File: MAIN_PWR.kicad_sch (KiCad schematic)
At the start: 0 parts

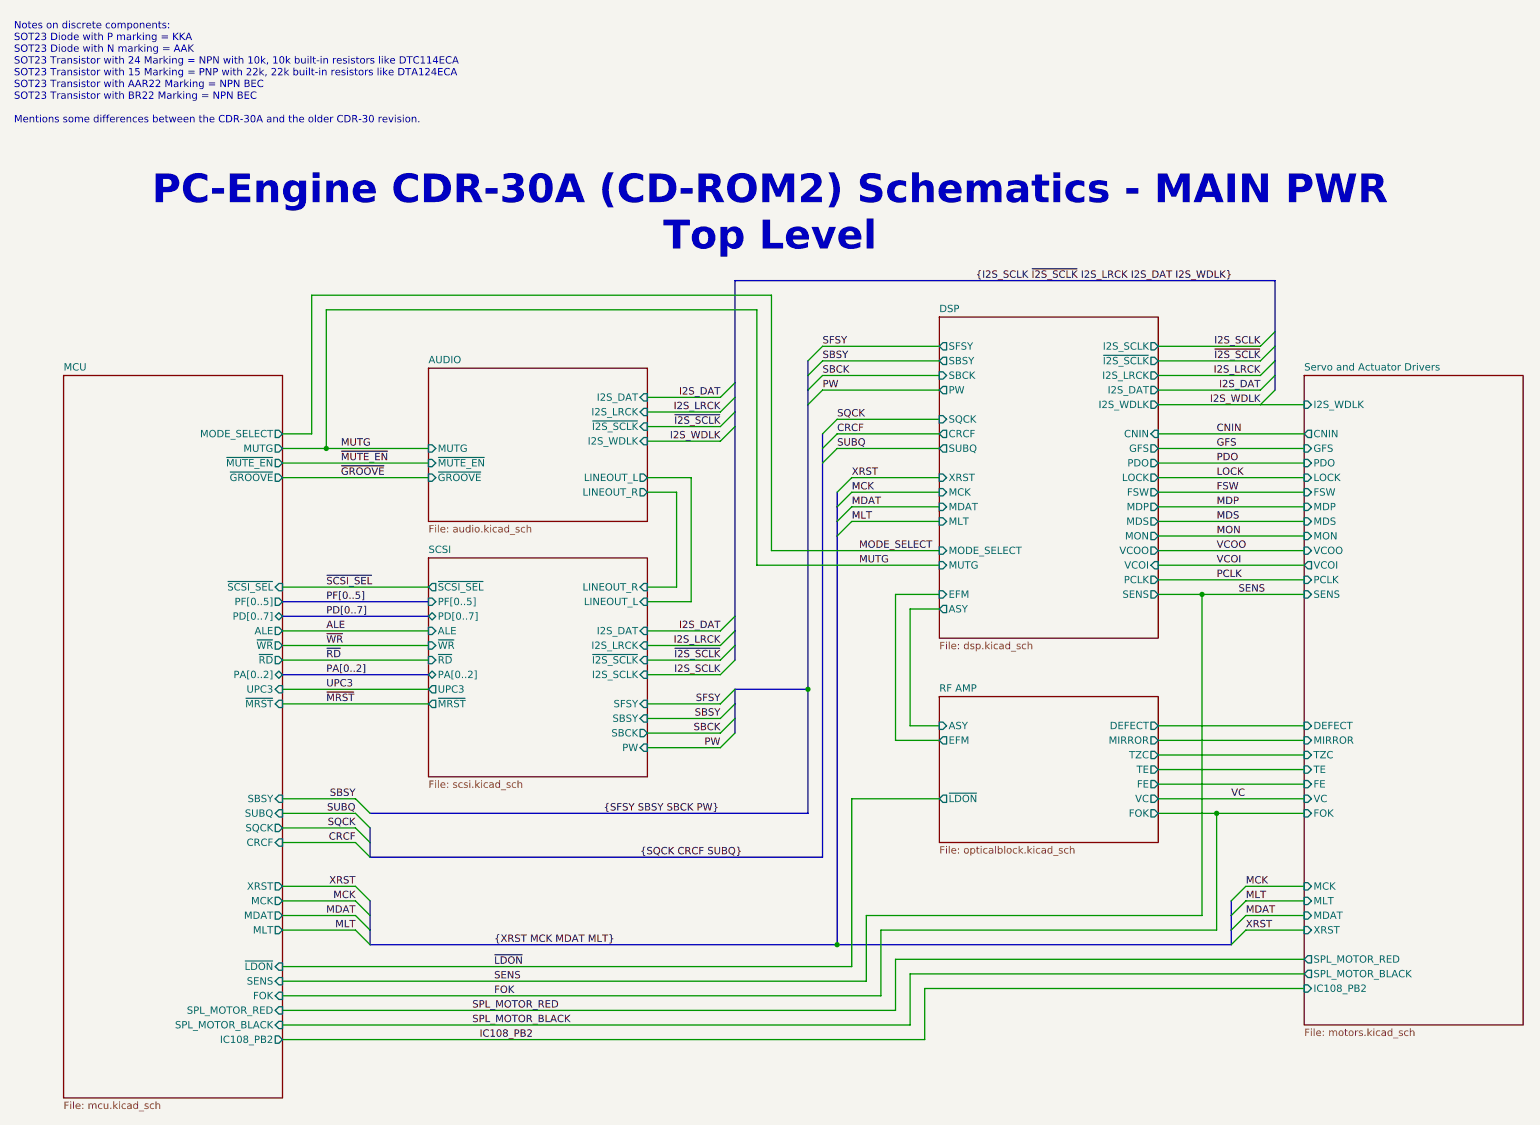
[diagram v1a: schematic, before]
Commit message: Small update, some typo fixes, more comments added to help understanding
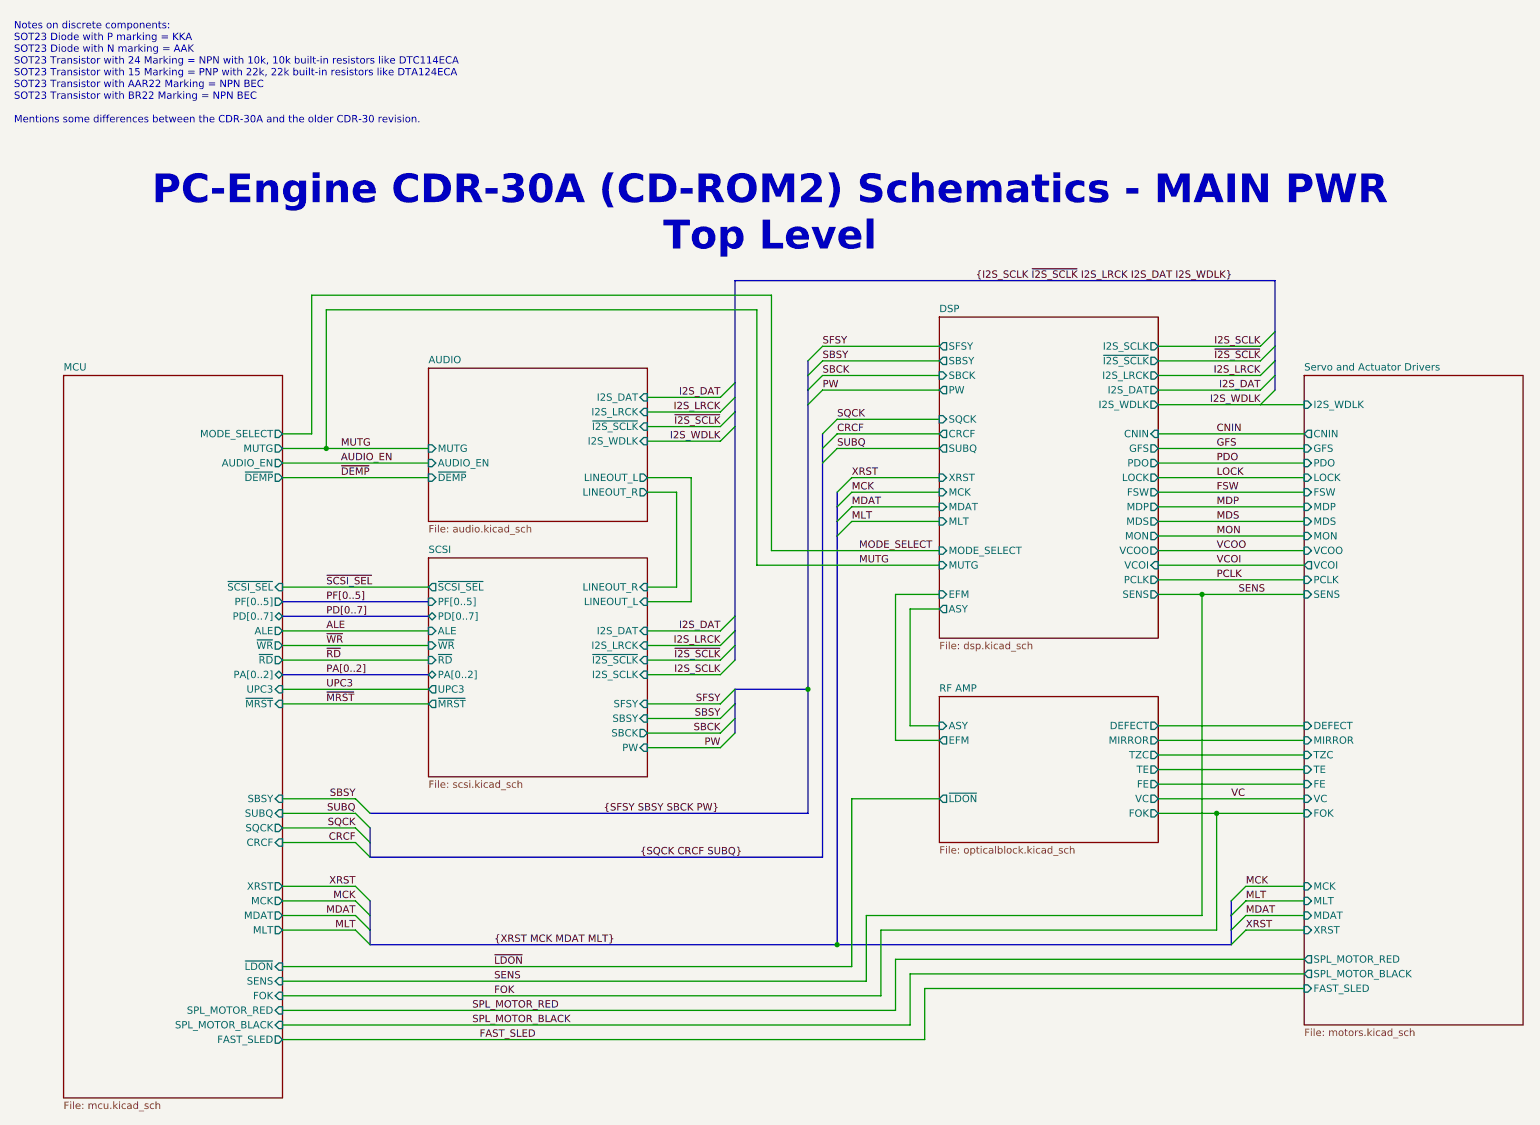
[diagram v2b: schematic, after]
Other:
- sheet AUDIO ports: added AUDIO_EN, ~{DEMP}; removed ~{GROOVE}, ~{MUTE_EN}
- sheet MCU ports: added AUDIO_EN, FAST_SLED, ~{DEMP}; removed IC108_PB2, ~{GROOVE}, ~{MUTE_EN}
- sheet Servo and Actuator Drivers ports: added FAST_SLED; removed IC108_PB2
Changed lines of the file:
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@@
 		)
 	)
-	(label "~{GROOVE}"
+	(label "~{DEMP}"
 		(at 73.66 68.58 0)
 		(fields_autoplaced yes)
@@
 		)
 	)
-	(label "IC108_PB2"
+	(label "FAST_SLED"
 		(at 97.79 166.37 0)
 		(fields_autoplaced yes)
@@
 		)
 	)
-	(label "~{MUTE_EN}"
+	(label "AUDIO_EN"
 		(at 73.66 66.04 0)
 		(fields_autoplaced yes)
@@
 			)
 		)
-		(pin "~{GROOVE}" output
+		(pin "~{DEMP}" output
 			(at 63.5 68.58 0)
 			(effects
@@
 			)
 		)
-		(pin "IC108_PB2" output
+		(pin "FAST_SLED" output
 			(at 63.5 166.37 0)
 			(effects
@@
 			)
 		)
-		(pin "~{MUTE_EN}" output
+		(pin "AUDIO_EN" output
 			(at 63.5 66.04 0)
 			(effects
@@
 			)
 		)
-		(pin "IC108_PB2" input
+		(pin "FAST_SLED" input
 			(at 241.3 157.48 180)
 			(effects
@@
 			)
 		)
-		(pin "~{MUTE_EN}" input
+		(pin "AUDIO_EN" input
 			(at 88.9 66.04 180)
 			(effects
@@
 			)
 		)
-		(pin "~{GROOVE}" input
+		(pin "~{DEMP}" input
 			(at 88.9 68.58 180)
 			(effects

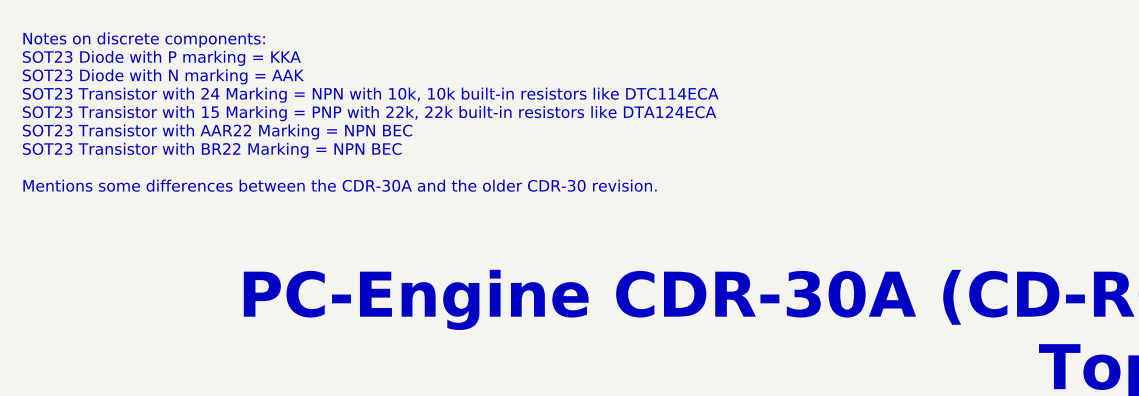
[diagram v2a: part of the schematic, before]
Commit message: KSS-220A Flexible PCBs ready and on order for trial.
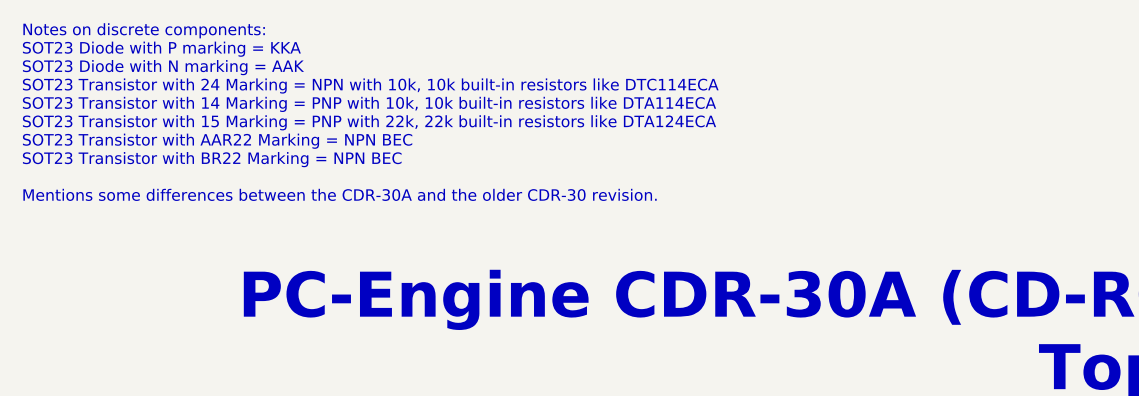
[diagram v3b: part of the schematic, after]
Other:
- note added: "Notes on discrete components: SOT23 Diode with P marking = KKA SOT23 Diode with N marking = AAK SOT23 Transistor with 24 Marking = NPN with 10k, 10k built-in resistors like DTC114ECA SOT23 Transistor with 14 Marking = PNP with 10k, 10k built-in resistors like DTA114ECA SOT23 Transistor with 15 Marking = PNP with 22k, 22k built-in resistors like DTA124ECA SOT23 Transistor with AAR22 Marking = NPN 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"
- note removed: "Notes on discrete components: SOT23 Diode with P marking = KKA SOT23 Diode with N marking = AAK SOT23 Transistor with 24 Marking = NPN with 10k, 10k built-in resistors like DTC114ECA SOT23 Transistor with 15 Marking = PNP with 22k, 22k built-in resistors like DTA124ECA SOT23 Transistor with AAR22 Marking = NPN BEC SOT23 Transistor with BR22 Marking = NPN BEC Mentions some differences between the 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"
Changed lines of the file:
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@@
 		)
 	)
-	(text "Notes on discrete components:\nSOT23 Diode with P marking = KKA\nSOT23 Diode with N marking = AAK\nSOT23 Transistor with 24 Marking = NPN with 10k, 10k built-in resistors like DTC114ECA\nSOT23 Transistor with 15 Marking = PNP with 22k, 22k built-in resistors like DTA124ECA\nSOT23 Transistor with AAR22 Marking = NPN BEC\nSOT23 Transistor with BR22 Marking = NPN BEC\n\nMentions some differences between the CDR-30A and the older CDR-30 revision."
+	(text "Notes on discrete components:\nSOT23 Diode with P marking = KKA\nSOT23 Diode with N marking = AAK\nSOT23 Transistor with 24 Marking = NPN with 10k, 10k built-in resistors like DTC114ECA\nSOT23 Transistor with 14 Marking = PNP with 10k, 10k built-in resistors like DTA114ECA\nSOT23 Transistor with 15 Marking = PNP with 22k, 22k built-in resistors like DTA124ECA\nSOT23 Transistor with AAR22 Marking = NPN BEC\nSOT23 Transistor with BR22 Marking = NPN BEC\n\nMentions some differences between the CDR-30A and the older CDR-30 revision."
 		(exclude_from_sim no)
 		(at 16.764 -1.778 0)
